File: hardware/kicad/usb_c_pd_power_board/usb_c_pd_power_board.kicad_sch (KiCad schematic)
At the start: 0 parts

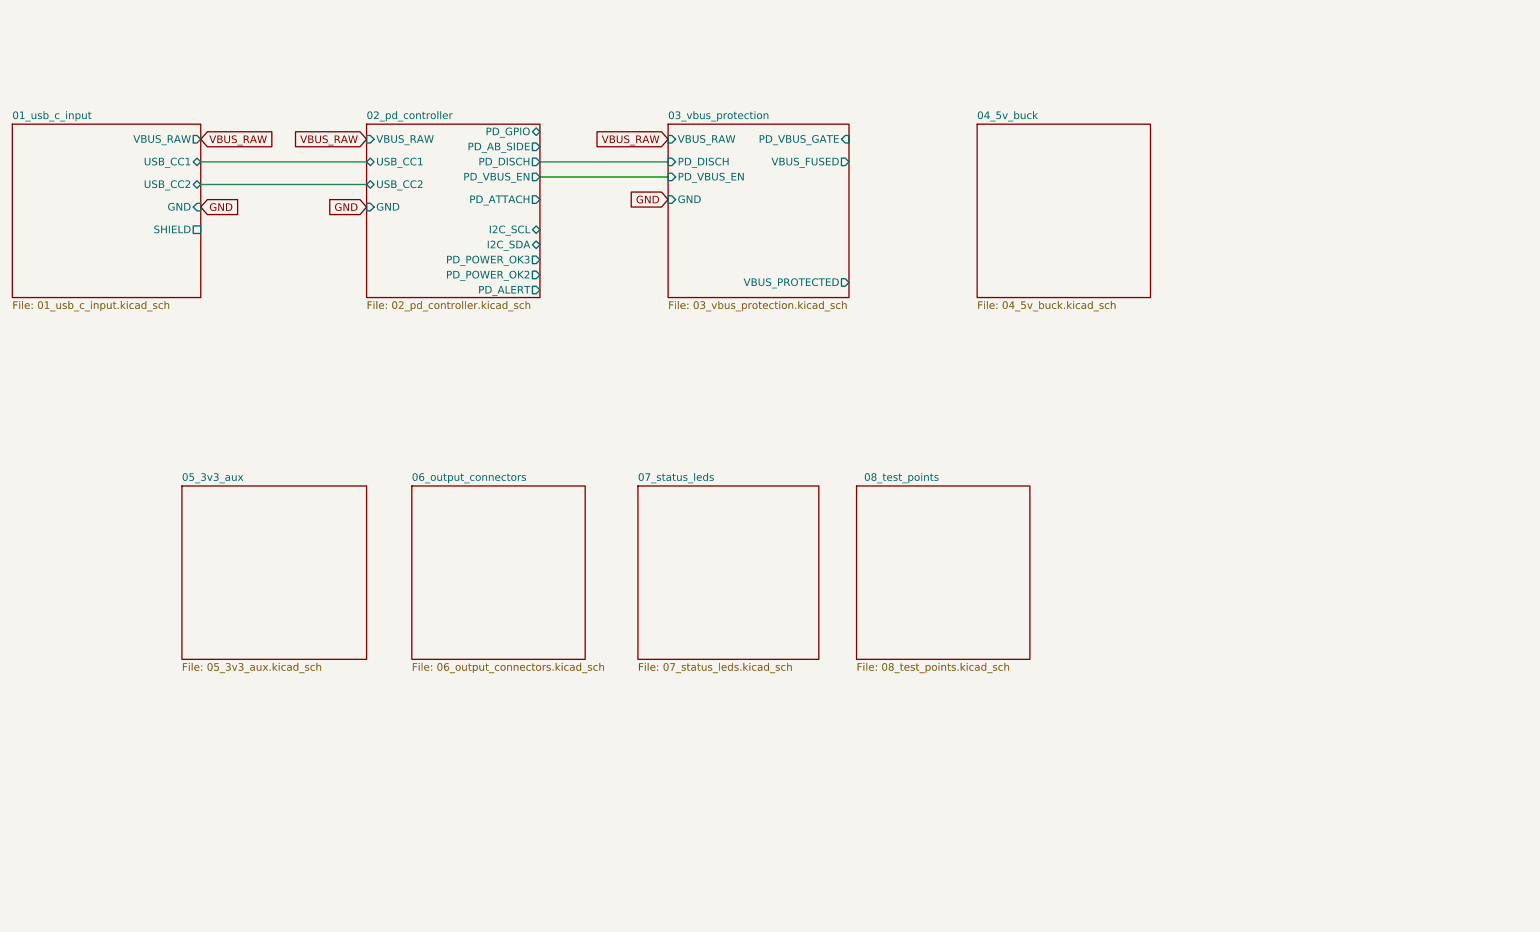
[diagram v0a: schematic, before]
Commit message: complete initial schematic and pass ERC
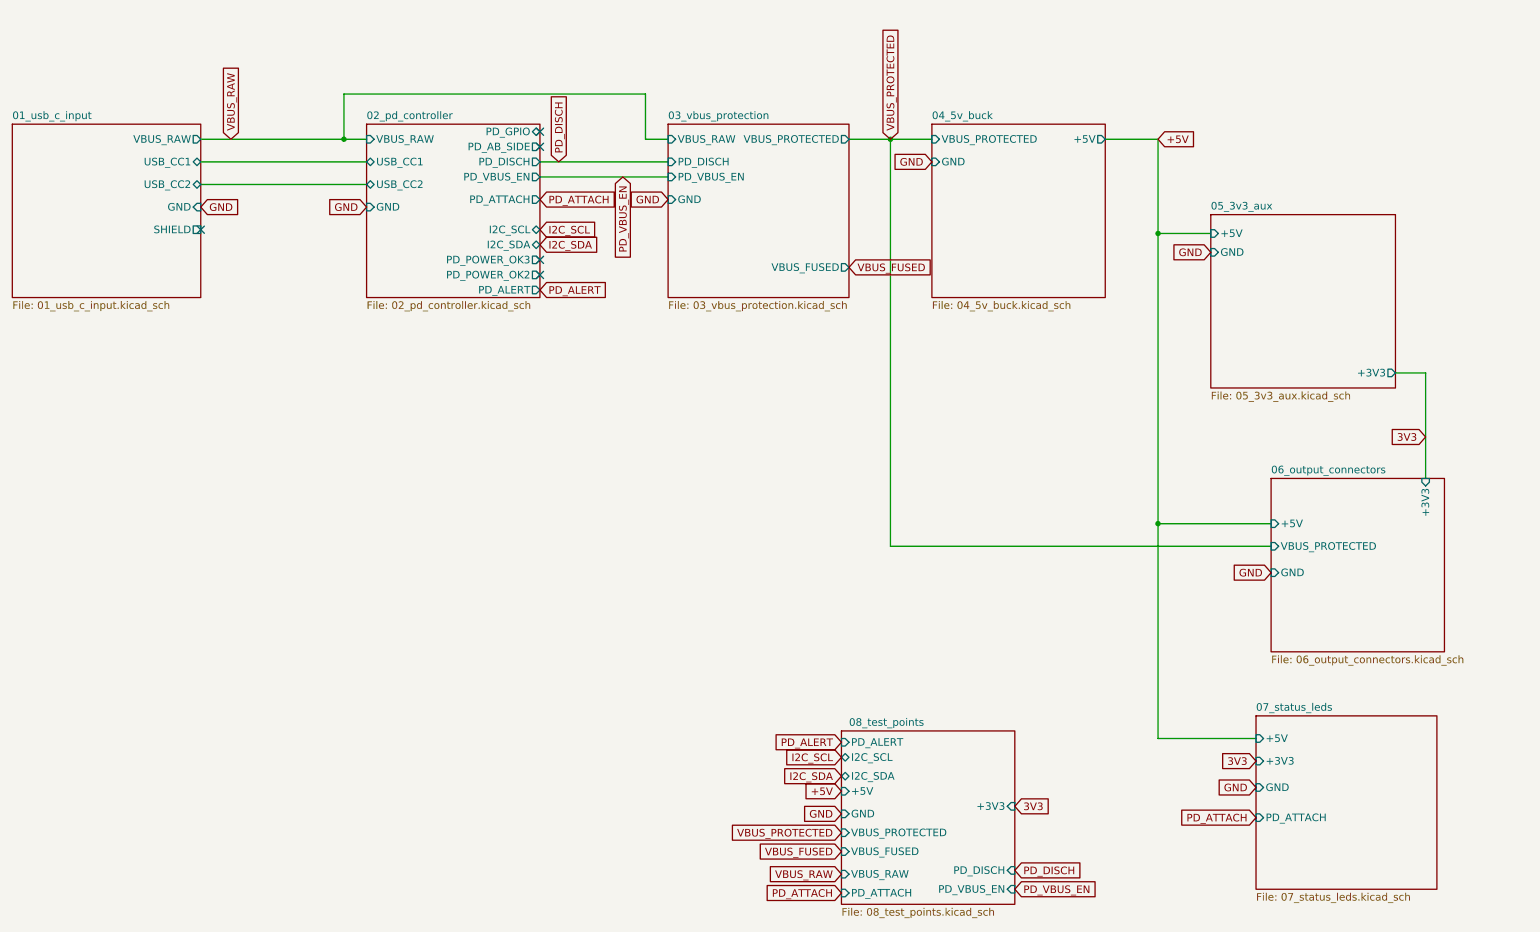
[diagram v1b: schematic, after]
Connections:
- no-connect marks 0 -> 5
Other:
- sheet 03_vbus_protection ports: added none; removed PD_VBUS_GATE
- sheet 04_5v_buck ports: added +5V, GND, VBUS_PROTECTED; removed none
- sheet 05_3v3_aux ports: added +3V3, +5V, GND; removed none
- sheet 06_output_connectors ports: added +3V3, +5V, GND, VBUS_PROTECTED; removed none
- sheet 07_status_leds ports: added +3V3, +5V, GND, PD_ATTACH; removed none
- sheet 08_test_points ports: added +3V3, +5V, GND, I2C_SCL, I2C_SDA, PD_ALERT, PD_ATTACH, PD_DISCH, PD_VBUS_EN, VBUS_FUSED, VBUS_PROTECTED, VBUS_RAW; removed none
